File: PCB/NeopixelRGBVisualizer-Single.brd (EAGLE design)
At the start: 36.2 x 36.1 mm, 23 parts, among them IC1 MSGEQ7, Q1 16MHz, X1 STEREOJACK

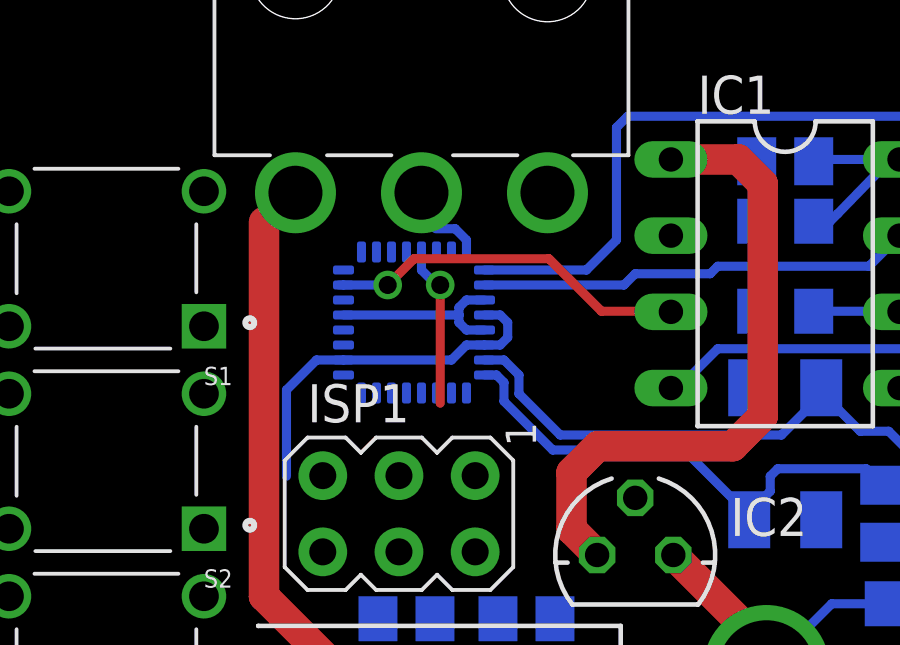
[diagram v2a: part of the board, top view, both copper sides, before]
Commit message: Updated broken ATMega328PB footprint.  This was caused by some Eagle glitch.
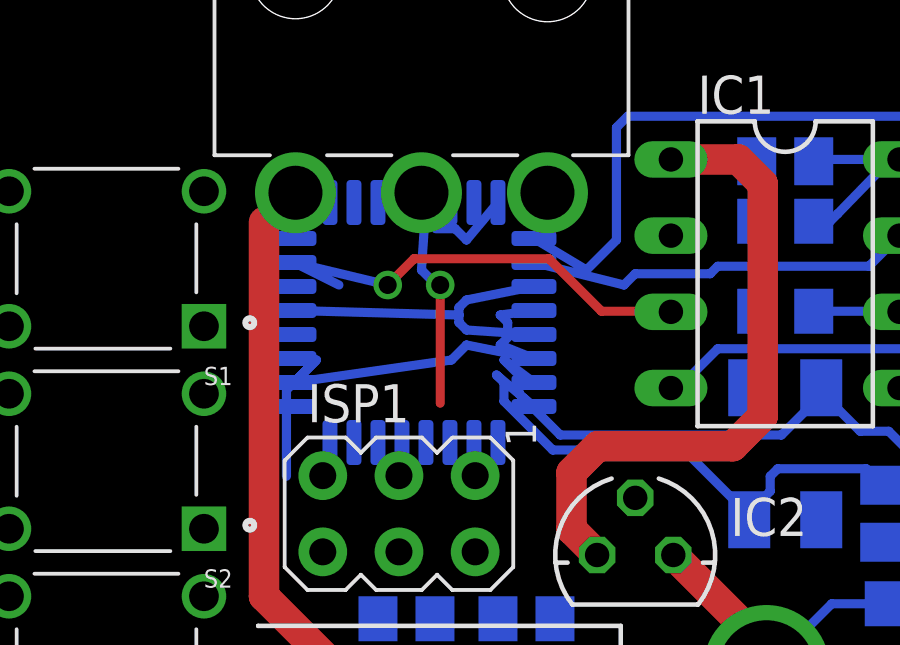
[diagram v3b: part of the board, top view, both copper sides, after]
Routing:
- net GND: track 6.26 -> 11.3 mm
- net VCC: track 36.7 -> 41.6 mm
- net N$7: track 12.2 -> 15.4 mm
- net N$2: track 5.37 -> 7.03 mm
- net N$9: track 14.5 -> 13.0 mm
- net N$8: track 37.1 -> 35.7 mm
- net N$17: track 1.58 -> 2.81 mm
- net N$15: track 17.1 -> 18.3 mm
- net N$14: track 19.1 -> 19.7 mm
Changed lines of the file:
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@@
 <contactref element="U$1" pad="17"/>
 <contactref element="ISP1" pad="3"/>
-<wire x1="15.75" y1="16.77" x2="13.9" y2="20.125" width="0" layer="19" extent="16-16"/>
+<wire x1="15.75" y1="16.77" x2="12.25" y2="19.075" width="0" layer="19" extent="16-16"/>
 </signal>
 <signal name="N$2">
@@
 <wire x1="17.125" y1="23.125" x2="17" y2="23.125" width="0.3048" layer="16"/>
 <wire x1="17" y1="23.125" x2="16.5" y2="23.625" width="0.3048" layer="16"/>
-<wire x1="16.5" y1="24.225" x2="16.5" y2="23.625" width="0.3048" layer="16"/>
+<wire x1="16.65" y1="25.875" x2="16.5" y2="23.625" width="0.3048" layer="16"/>
 <wire x1="17.125" y1="23.125" x2="17.125" y2="19.185" width="0.3048" layer="1"/>
 <wire x1="17.125" y1="19.185" x2="13.21" y2="16.77" width="0" layer="19" extent="1-1"/>
@@
 <contactref element="U$1" pad="16"/>
 <contactref element="ISP1" pad="1"/>
-<wire x1="18.29" y1="16.77" x2="14.5" y2="19.525" width="0" layer="19" extent="16-16"/>
+<wire x1="18.29" y1="16.77" x2="13.45" y2="17.875" width="0" layer="19" extent="16-16"/>
 </signal>
 <signal name="N$4">
 <contactref element="ISP1" pad="4"/>
 <contactref element="U$1" pad="15"/>
-<wire x1="15.75" y1="14.23" x2="15" y2="19.525" width="0" layer="19" extent="16-16"/>
+<wire x1="15.75" y1="14.23" x2="14.25" y2="17.875" width="0" layer="19" extent="16-16"/>
 </signal>
 <signal name="N$7">
@@
 <contactref element="IC1" pad="3"/>
 <via x="15.375" y="23.125" extent="1-16" drill="0.6"/>
-<wire x1="13.9" y1="23.125" x2="13.75" y2="23.125" width="0.3048" layer="16"/>
-<wire x1="15.375" y1="23.125" x2="13.9" y2="23.125" width="0.3048" layer="16"/>
+<wire x1="12.25" y1="23.875" x2="13.75" y2="23.125" width="0.3048" layer="16"/>
+<wire x1="15.375" y1="23.125" x2="12.25" y2="23.875" width="0.3048" layer="16"/>
 <wire x1="20.75" y1="24" x2="16.25" y2="24" width="0.3048" layer="1"/>
 <wire x1="22.5" y1="22.25" x2="20.75" y2="24" width="0.3048" layer="1"/>
@@
 <wire x1="34.375" y1="27.75" x2="33.375" y2="28.75" width="0.3048" layer="16"/>
 <wire x1="33.375" y1="28.75" x2="23.375" y2="28.75" width="0.3048" layer="16"/>
-<wire x1="22" y1="23.625" x2="18.6" y2="23.625" width="0.3048" layer="16"/>
+<wire x1="22" y1="23.625" x2="20.25" y2="24.675" width="0.3048" layer="16"/>
 <wire x1="23.375" y1="28.75" x2="23" y2="28.375" width="0.3048" layer="16"/>
 <wire x1="23" y1="28.375" x2="23" y2="24.625" width="0.3048" layer="16"/>
@@
 <contactref element="U$1" pad="2"/>
 <contactref element="IC1" pad="7"/>
-<wire x1="23.25" y1="23.125" x2="18.6" y2="23.125" width="0.3048" layer="16"/>
+<wire x1="23.25" y1="23.125" x2="20.25" y2="23.875" width="0.3048" layer="16"/>
 <wire x1="23.625" y1="23.5" x2="23.25" y2="23.125" width="0.3048" layer="16"/>
 <wire x1="26.125" y1="23.5" x2="23.625" y2="23.5" width="0.3048" layer="16"/>
@@
 </polygon>
 <contactref element="X1" pad="1"/>
-<wire x1="18.6" y1="22.625" x2="18" y2="22.625" width="0.3048" layer="16"/>
+<wire x1="20.25" y1="23.075" x2="18" y2="22.625" width="0.3048" layer="16"/>
 <wire x1="18" y1="22.625" x2="17.75" y2="22.375" width="0.3048" layer="16"/>
 <wire x1="17.75" y1="22.375" x2="17.75" y2="22.125" width="0.3048" layer="16"/>
 <wire x1="17.75" y1="22.125" x2="17.75" y2="21.875" width="0.3048" layer="16"/>
 <wire x1="18" y1="21.625" x2="17.75" y2="21.875" width="0.3048" layer="16"/>
-<wire x1="18.6" y1="21.625" x2="18" y2="21.625" width="0.3048" layer="16"/>
-<wire x1="17.75" y1="22.125" x2="13.9" y2="22.125" width="0.3048" layer="16"/>
+<wire x1="20.25" y1="21.475" x2="18" y2="21.625" width="0.3048" layer="16"/>
+<wire x1="17.75" y1="22.125" x2="12.25" y2="22.275" width="0.3048" layer="16"/>
 <contactref element="C8" pad="2"/>
 <contactref element="IC2" pad="GND"/>
@@
 <wire x1="24.815" y1="24.77" x2="27.675" y2="25.25" width="0" layer="19" extent="16-16"/>
 <wire x1="27.675" y1="22.25" x2="27.675" y2="25.25" width="0" layer="19" extent="16-16"/>
-<wire x1="18.6" y1="22.625" x2="24.815" y2="24.77" width="0" layer="19" extent="16-16"/>
-<wire x1="13.21" y1="14.23" x2="18.6" y2="21.625" width="0" layer="19" extent="16-16"/>
+<wire x1="20.25" y1="23.075" x2="24.815" y2="24.77" width="0" layer="19" extent="16-16"/>
+<wire x1="13.21" y1="14.23" x2="20.25" y2="21.475" width="0" layer="19" extent="16-16"/>
 <wire x1="20.95" y1="12" x2="13.21" y2="14.23" width="0" layer="19" extent="16-16"/>
 <wire x1="15.05" y1="12" x2="20.95" y2="12" width="0" layer="19" extent="16-16"/>
@@
 <wire x1="32.8" y1="7.5" x2="33.825" y2="12.5" width="0" layer="19" extent="16-16"/>
 <wire x1="28" y1="4.1" x2="32.8" y2="7.5" width="0" layer="19" extent="1-1"/>
-<wire x1="2.75" y1="19.5" x2="13.9" y2="22.125" width="0" layer="19" extent="16-16"/>
+<wire x1="2.75" y1="19.5" x2="12.25" y2="22.275" width="0" layer="19" extent="16-16"/>
 <wire x1="2.75" y1="21.75" x2="2.75" y2="19.5" width="0" layer="19" extent="1-1"/>
 <wire x1="2.75" y1="26.25" x2="2.75" y2="21.75" width="0" layer="19" extent="1-1"/>
@@
 <contactref element="U$1" pad="7"/>
 <contactref element="C5" pad="2"/>
-<wire x1="19.25" y1="20.625" x2="18.6" y2="20.625" width="0.3048" layer="16"/>
+<wire x1="19.25" y1="20.625" x2="20.25" y2="19.875" width="0.3048" layer="16"/>
 <wire x1="19.75" y1="20.125" x2="19.25" y2="20.625" width="0.3048" layer="16"/>
 <wire x1="19.75" y1="20.125" x2="19.75" y2="19.5" width="0.3048" layer="16"/>
@@
 <contactref element="U$1" pad="8"/>
 <contactref element="C6" pad="2"/>
-<wire x1="19" y1="20.125" x2="18.6" y2="20.125" width="0.3048" layer="16"/>
+<wire x1="19" y1="20.125" x2="20.25" y2="19.075" width="0.3048" layer="16"/>
 <wire x1="19.25" y1="19.875" x2="19" y2="20.125" width="0.3048" layer="16"/>
 <wire x1="19.25" y1="19.875" x2="19.25" y2="19.25" width="0.3048" layer="16"/>
@@
 <signal name="N$17">
 <contactref element="U$1" pad="32"/>
-<wire x1="18" y1="24.625" x2="18" y2="24.225" width="0.3048" layer="16"/>
+<wire x1="18" y1="24.625" x2="19.05" y2="25.875" width="0.3048" layer="16"/>
 <wire x1="18" y1="24.625" x2="17.625" y2="25" width="0.3048" layer="16"/>
 <wire x1="17.625" y1="25" x2="16.975" y2="25" width="0.3048" layer="16"/>
@@
 <wire x1="27.675" y1="27.25" x2="24.875" y2="27.25" width="0.3048" layer="16"/>
 <wire x1="13" y1="20.625" x2="12" y2="19.625" width="0.3048" layer="16"/>
-<wire x1="13.9" y1="20.625" x2="13" y2="20.625" width="0.3048" layer="16"/>
+<wire x1="12.25" y1="19.875" x2="13" y2="20.625" width="0.3048" layer="16"/>
 <wire x1="12" y1="19.625" x2="12" y2="16.75" width="0.3048" layer="16"/>
-<wire x1="18.6" y1="21.125" x2="18" y2="21.125" width="0.3048" layer="16"/>
+<wire x1="20.25" y1="20.675" x2="18" y2="21.125" width="0.3048" layer="16"/>
 <wire x1="18" y1="21.125" x2="17.5" y2="20.625" width="0.3048" layer="16"/>
-<wire x1="17.5" y1="20.625" x2="13.9" y2="20.625" width="0.3048" layer="16"/>
-<wire x1="19.125" y1="22.125" x2="18.6" y2="22.125" width="0.3048" layer="16"/>
+<wire x1="17.5" y1="20.625" x2="12.25" y2="19.875" width="0.3048" layer="16"/>
+<wire x1="19.125" y1="22.125" x2="20.25" y2="22.275" width="0.3048" layer="16"/>
 <wire x1="19.375" y1="21.875" x2="19.125" y2="22.125" width="0.3048" layer="16"/>
 <wire x1="19.375" y1="21.875" x2="19.375" y2="21.375" width="0.3048" layer="16"/>
 <wire x1="19.375" y1="21.375" x2="19.125" y2="21.125" width="0.3048" layer="16"/>
-<wire x1="19.125" y1="21.125" x2="18.6" y2="21.125" width="0.3048" layer="16"/>
+<wire x1="19.125" y1="21.125" x2="20.25" y2="20.675" width="0.3048" layer="16"/>
 <wire x1="24.875" y1="27.25" x2="24.815" y2="27.31" width="0.8128" layer="1"/>
 <contactref element="IC2" pad="OUT"/>
@@
 <contactref element="U$1" pad="11"/>
 <wire x1="9.25" y1="21.75" x2="9.25" y2="26.25" width="0" layer="19" extent="1-1"/>
-<wire x1="17" y1="19.525" x2="9.25" y2="21.75" width="0" layer="19" extent="16-16"/>
+<wire x1="17.45" y1="17.875" x2="9.25" y2="21.75" width="0" layer="19" extent="16-16"/>
 </signal>
 <signal name="N$19">
@@
 <contactref element="S2" pad="2"/>
 <contactref element="U$1" pad="10"/>
-<wire x1="9.25" y1="19.5" x2="17.5" y2="19.525" width="0" layer="19" extent="16-16"/>
+<wire x1="9.25" y1="19.5" x2="18.25" y2="17.875" width="0" layer="19" extent="16-16"/>
 <wire x1="9.25" y1="15" x2="9.25" y2="19.5" width="0" layer="19" extent="1-1"/>
 </signal>
@@
 <contactref element="S3" pad="2"/>
 <contactref element="U$1" pad="9"/>
-<wire x1="9.25" y1="12.75" x2="18" y2="19.525" width="0" layer="19" extent="16-16"/>
+<wire x1="9.25" y1="12.75" x2="19.05" y2="17.875" width="0" layer="19" extent="16-16"/>
 <wire x1="9.25" y1="8.25" x2="9.25" y2="12.75" width="0" layer="19" extent="1-1"/>
 </signal>

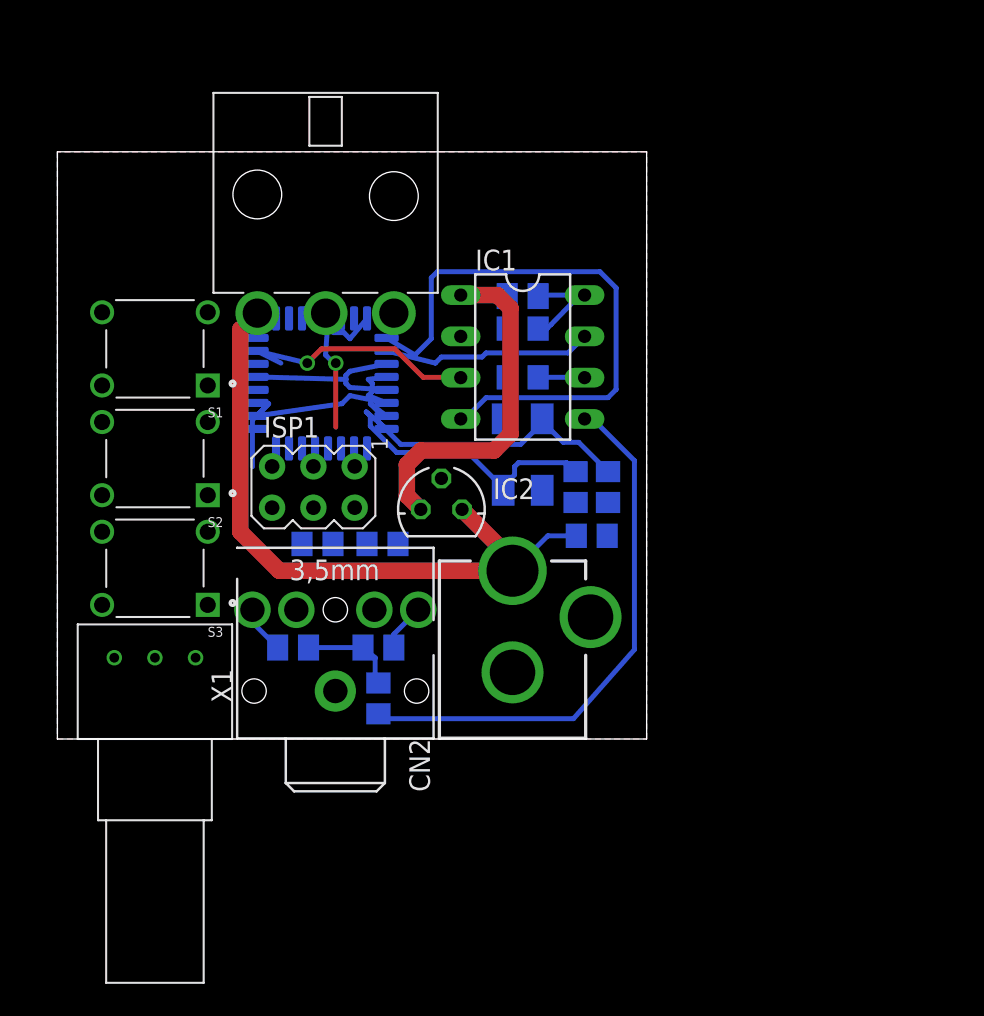
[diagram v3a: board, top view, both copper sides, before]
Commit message: Very tight design, needs to be fit into a larger enclosure.
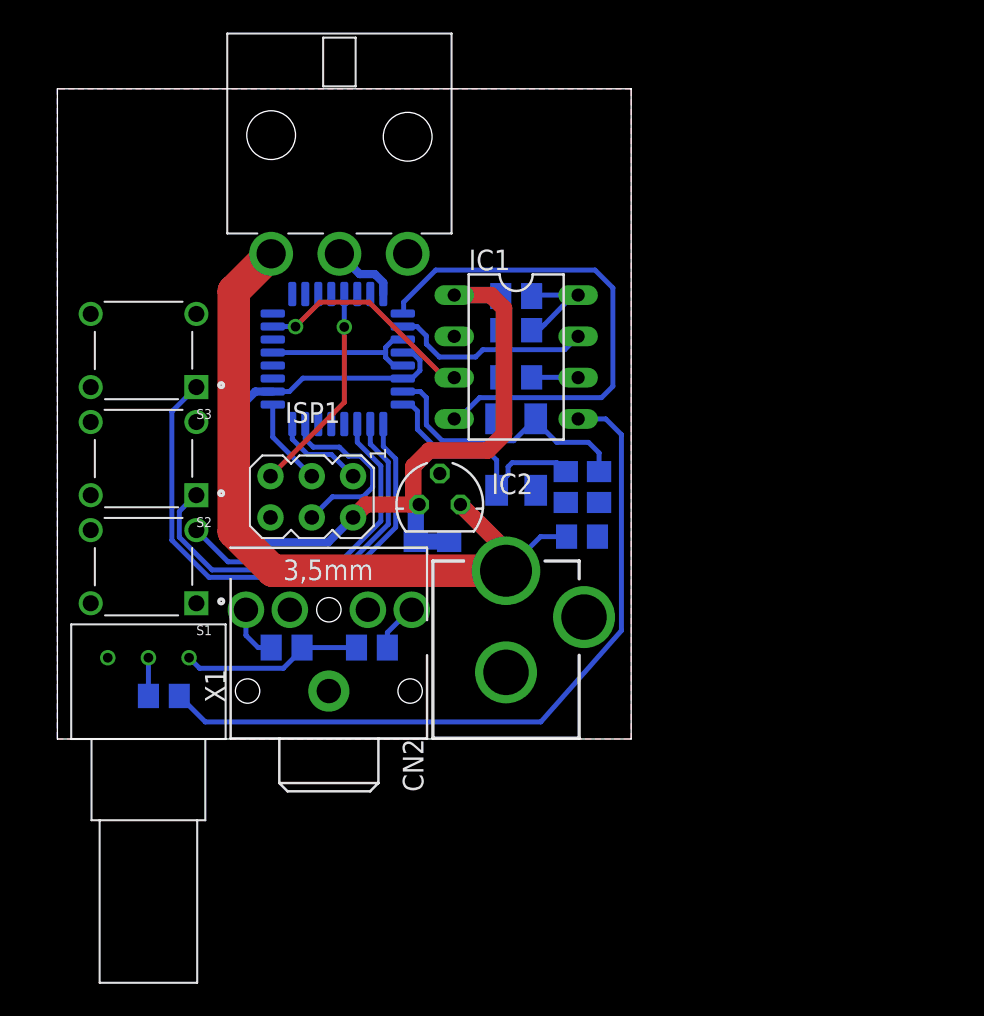
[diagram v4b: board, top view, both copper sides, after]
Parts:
- CN2: value (none) -> 5-12VDC
- IC2: value (none) -> 78L05ACZ-AP
- moved S1 13.4 mm to (5.30, 10.6)
- moved S3 13.4 mm to (5.30, 23.9)
- moved C1 13.2 mm to (6.55, 2.65), turned to 180 degrees
- moved C7 8.14 mm to (24.1, 11.2), turned to 270 degrees
- moved U$3 3.75 mm to (17.4, 37.1)
- moved C3 2.20 mm to (22.1, 11.2), turned to 270 degrees
- moved U$1 1.80 mm to (17.2, 23.4)
- moved S2 0.70 mm to (5.30, 17.2)
- moved ISP1 0.61 mm to (15.7, 14.9)
- moved C8 0.60 mm to (32.3, 12.4)
- moved C6 0.60 mm to (31.3, 15.5)
- moved C5 0.55 mm to (33.3, 15.5)
- moved C2 0.41 mm to (28.2, 25.1)
- moved R2 0.40 mm to (14.1, 5.62)
- moved U$2 0.40 mm to (5.60, 0.00)
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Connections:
- net N$18: no longer S1.1
- net N$19: no longer S2.2
- net N$20: no longer S3.2
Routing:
- net N$20: track 0.00 -> 32.7 mm
- net N$19: track 0.00 -> 24.5 mm
- net N$18: track 0.00 -> 19.8 mm
- net VCC: track 41.6 -> 60.8 mm
- net N$10: track 33.6 -> 45.5 mm
- net N$4: track 0.00 -> 11.5 mm
- net N$2: track 7.03 -> 13.1 mm
- net N$3: track 0.00 -> 5.61 mm
- net N$6: track 5.60 -> 11.2 mm
- net VIN: track 40.1 -> 45.6 mm
- net N$1: track 0.00 -> 5.40 mm
- net N$8: track 35.7 -> 31.5 mm
- net N$15: track 18.3 -> 15.3 mm
- net N$14: track 19.7 -> 17.0 mm
- net N$16: track 0.00 -> 2.35 mm
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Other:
- board size 36.2 x 36.1 mm -> 35.3 x 40 mm

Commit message: Reorganized and resized board to match new project box dimensions.
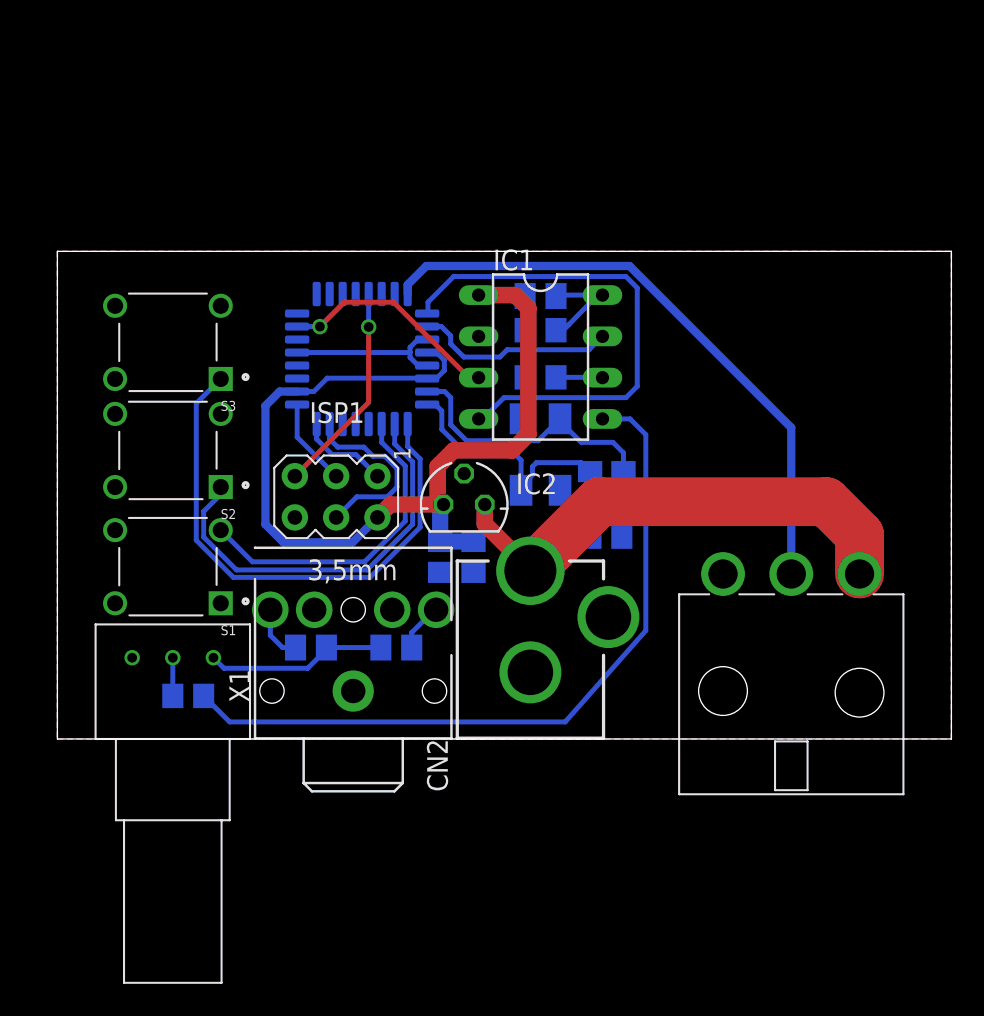
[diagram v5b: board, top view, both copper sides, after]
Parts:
- moved U$3 44.2 mm to (45.1, 2.85), turned to 0 degrees
- moved S2 1.58 mm to (6.80, 17.8)
- moved S3 1.58 mm to (6.80, 24.4)
- moved C1 1.50 mm to (8.05, 2.65)
- moved C2 1.50 mm to (29.7, 25.1)
- moved C3 1.50 mm to (23.6, 11.2)
- moved C4 1.50 mm to (29.7, 22.2)
- moved C5 1.50 mm to (34.8, 15.5)
- moved C6 1.50 mm to (32.8, 15.5)
- moved C7 1.50 mm to (25.6, 11.2)
- moved C8 1.50 mm to (33.8, 12.4)
- moved CN2 1.50 mm to (29.1, -3.25)
- moved IC1 1.50 mm to (29.7, 23.5)
- moved IC2 1.50 mm to (25.0, 14.4)
- moved Q1 1.50 mm to (29.7, 17.5)
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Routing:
- net N$17: track 4.14 -> 37.8 mm
- net VIN: track 45.6 -> 35.1 mm
- net N$20: track 32.7 -> 33.2 mm
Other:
- board size 35.3 x 40 mm -> 55 x 30 mm
